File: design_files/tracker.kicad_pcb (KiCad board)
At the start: 4 copper layers, 49.4 x 53.4 mm, 88 parts, among them J1 Conn_01x01, J2 Conn_01x01, J3 Conn_01x05, J4 Conn_Coaxial, J5 SIM_Card, J6 Conn_01x02, M1 BG96, Q1 DMP2008UFG, U1 STM32U545CEUx, U10 PUMH10,115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

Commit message: Edits
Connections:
- U12 pad 2: /I2C_SDA -> +3V3
- U12 pad 3: unconnected-(U12-DOUT_A6-Pad3) -> +3V3
- U12 pad 4: unconnected-(U12-DIN_SDA-Pad4) -> /I2C_SDA
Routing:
- net +3V3: track 58.1 -> 61.1 mm
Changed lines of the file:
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@@
 	(net 144 "Net-(U11-~{QON})")
 	(net 145 "Net-(U11-~{CE})")
-	(net 146 "unconnected-(U12-DIN_SDA-Pad4)")
-	(net 147 "unconnected-(U12-NC-Pad5)")
-	(net 148 "unconnected-(U12-NC-Pad10)")
-	(net 149 "unconnected-(U12-INTN2-Pad11)")
-	(net 150 "unconnected-(U12-DOUT_A6-Pad3)")
-	(net 151 "unconnected-(U12-NC-Pad8)")
-	(net 152 "/accelerometer/ACC_INT1")
-	(net 153 "unconnected-(Y1-Pad2)")
-	(net 154 "unconnected-(Y1-Pad3)")
+	(net 146 "unconnected-(U12-NC-Pad5)")
+	(net 147 "unconnected-(U12-NC-Pad10)")
+	(net 148 "unconnected-(U12-INTN2-Pad11)")
+	(net 149 "unconnected-(U12-NC-Pad8)")
+	(net 150 "/accelerometer/ACC_INT1")
+	(net 151 "unconnected-(Y1-Pad2)")
+	(net 152 "unconnected-(Y1-Pad3)")
 	(footprint "Resistor_SMD:R_0603_1608Metric"
 		(layer "F.Cu")
@@
 			(layers "F.Cu" "F.Mask" "F.Paste")
 			(roundrect_rratio 0.25)
-			(net 153 "unconnected-(Y1-Pad2)")
+			(net 151 "unconnected-(Y1-Pad2)")
 			(pinfunction "2")
 			(pintype "passive+no_connect")
@@
 			(layers "F.Cu" "F.Mask" "F.Paste")
 			(roundrect_rratio 0.25)
-			(net 154 "unconnected-(Y1-Pad3)")
+			(net 152 "unconnected-(Y1-Pad3)")
 			(pinfunction "3")
 			(pintype "passive+no_connect")
@@
 			(layers "F.Cu" "F.Mask" "F.Paste")
 			(roundrect_rratio 0.25)
-			(net 152 "/accelerometer/ACC_INT1")
+			(net 150 "/accelerometer/ACC_INT1")
 			(pinfunction "PA8")
 			(pintype "bidirectional")
@@
 			(size 0.375 0.35)
 			(layers "B.Cu" "B.Mask" "B.Paste")
-			(net 133 "/I2C_SDA")
+			(net 6 "+3V3")
 			(pinfunction "CSN")
 			(pintype "input")
@@
 			(size 0.375 0.35)
 			(layers "B.Cu" "B.Mask" "B.Paste")
-			(net 150 "unconnected-(U12-DOUT_A6-Pad3)")
+			(net 6 "+3V3")
 			(pinfunction "DOUT_A6")
-			(pintype "output+no_connect")
+			(pintype "output")
 		)
 		(pad "4" smd rect
@@
 			(size 0.375 0.35)
 			(layers "B.Cu" "B.Mask" "B.Paste")
-			(net 146 "unconnected-(U12-DIN_SDA-Pad4)")
+			(net 133 "/I2C_SDA")
 			(pinfunction "DIN_SDA")
-			(pintype "input+no_connect")
+			(pintype "input")
 		)
 		(pad "5" smd rect
@@
 			(size 0.375 0.35)
 			(layers "B.Cu" "B.Mask" "B.Paste")
-			(net 147 "unconnected-(U12-NC-Pad5)")
+			(net 146 "unconnected-(U12-NC-Pad5)")
 			(pinfunction "NC")
 			(pintype "no_connect")
@@
 			(size 0.375 0.35)
 			(layers "B.Cu" "B.Mask" "B.Paste")
-			(net 151 "unconnected-(U12-NC-Pad8)")
+			(net 149 "unconnected-(U12-NC-Pad8)")
 			(pinfunction "NC")
 			(pintype "no_connect")
@@
 			(size 0.375 0.35)
 			(layers "B.Cu" "B.Mask" "B.Paste")
-			(net 148 "unconnected-(U12-NC-Pad10)")
+			(net 147 "unconnected-(U12-NC-Pad10)")
 			(pinfunction "NC")
 			(pintype "no_connect")
@@
 			(size 0.375 0.35)
 			(layers "B.Cu" "B.Mask" "B.Paste")
-			(net 149 "unconnected-(U12-INTN2-Pad11)")
+			(net 148 "unconnected-(U12-INTN2-Pad11)")
 			(pinfunction "INTN2")
 			(pintype "output+no_connect")
@@
 			(size 0.375 0.35)
 			(layers "B.Cu" "B.Mask" "B.Paste")
-			(net 152 "/accelerometer/ACC_INT1")
+			(net 150 "/accelerometer/ACC_INT1")
 			(pinfunction "INTN1")
 			(pintype "output")
@@
 	)
 	(via
-		(at 144.53 85.2)
+		(at 144.5 84.55)
 		(size 0.6)
 		(drill 0.3)
@@
 	)
 	(segment
+		(start 135.25 84.69)
+		(end 135.4 84.54)
+		(width 0.15)
+		(layer "F.Cu")
+		(net 6)
+	)
+	(segment
 		(start 158.1325 82.51)
 		(end 158.1325 81.3475)
@@
 	)
 	(segment
-		(start 135.25 84.69)
-		(end 135.27 84.71)
-		(width 0.15)
-		(layer "F.Cu")
-		(net 6)
-	)
-	(segment
 		(start 138.99 86.21)
 		(end 138.99 85.67)
@@
 	)
 	(segment
+		(start 135.4 84.54)
+		(end 135.4 84.15)
+		(width 0.15)
+		(layer "F.Cu")
+		(net 6)
+	)
+	(segment
 		(start 138.99 85.67)
 		(end 138.47 85.15)
@@
 	)
 	(via
-		(at 135.27 84.71)
+		(at 135.4 84.15)
 		(size 0.6)
 		(drill 0.3)
@@
 	)
 	(segment
+		(start 135.3 84.05)
+		(end 135.4 84.15)
+		(width 0.15)
+		(layer "B.Cu")
+		(net 6)
+	)
+	(segment
 		(start 142.47 76.8875)
 		(end 141.7675 76.8875)
@@
 	)
 	(segment
+		(start 134.3125 84.05)
+		(end 134.3785 83.984)
+		(width 0.15)
+		(layer "B.Cu")
+		(net 6)
+	)
+	(segment
 		(start 157.68 81.34)
 		(end 158.14 81.34)
@@
 	)
 	(segment
+		(start 135 84.55)
+		(end 135.4 84.15)
+		(width 0.15)
+		(layer "B.Cu")
+		(net 6)
+	)
+	(segment
 		(start 131.655 84.455)
 		(end 131.655 84.345)
@@
 	)
 	(segment
+		(start 134.3125 84.55)
+		(end 135 84.55)
+		(width 0.15)
+		(layer "B.Cu")
+		(net 6)
+	)
+	(segment
+		(start 134.3125 84.05)
+		(end 135.3 84.05)
+		(width 0.15)
+		(layer "B.Cu")
+		(net 6)
+	)
+	(segment
 		(start 131.655 84.345)
 		(end 131.95 84.05)
@@
 	)
 	(segment
-		(start 134.3785 83.984)
-		(end 137.580123 83.984)
+		(start 137.580123 83.984)
+		(end 137.926123 84.33)
 		(width 0.15)
 		(layer "B.Cu")
@@
 	)
 	(segment
-		(start 137.580123 83.984)
-		(end 137.926123 84.33)
+		(start 134.3125 85.05)
+		(end 135.45 85.05)
 		(width 0.15)
 		(layer "B.Cu")
@@
 	)
 	(segment
-		(start 134.3125 84.05)
-		(end 134.3785 83.984)
+		(start 135.45 85.05)
+		(end 136.516 83.984)
+		(width 0.15)
+		(layer "B.Cu")
+		(net 133)
+	)
+	(segment
+		(start 136.516 83.984)
+		(end 137.580123 83.984)
 		(width 0.15)
 		(layer "B.Cu")
@@
 		(width 0.15)
 		(layer "F.Cu")
-		(net 152)
+		(net 150)
 	)
 	(segment
@@
 		(width 0.15)
 		(layer "F.Cu")
-		(net 152)
+		(net 150)
 	)
 	(segment
@@
 		(width 0.15)
 		(layer "F.Cu")
-		(net 152)
+		(net 150)
 	)
 	(segment
@@
 		(width 0.15)
 		(layer "F.Cu")
-		(net 152)
+		(net 150)
 	)
 	(segment
@@
 		(width 0.15)
 		(layer "F.Cu")
-		(net 152)
+		(net 150)
 	)
 	(via
@@
 		(drill 0.3)
 		(layers "F.Cu" "B.Cu")
-		(net 152)
+		(net 150)
 	)
 	(segment
@@
 		(width 0.15)
 		(layer "B.Cu")
-		(net 152)
+		(net 150)
 	)
 	(segment
@@
 		(width 0.15)
 		(layer "B.Cu")
-		(net 152)
+		(net 150)
 	)
 	(segment
@@
 		(width 0.15)
 		(layer "B.Cu")
-		(net 152)
+		(net 150)
 	)
 	(segment
@@
 		(width 0.15)
 		(layer "B.Cu")
-		(net 152)
+		(net 150)
 	)
 	(segment
@@
 		(width 0.15)
 		(layer "B.Cu")
-		(net 152)
+		(net 150)
 	)
 	(segment
@@
 		(width 0.15)
 		(layer "B.Cu")
-		(net 152)
+		(net 150)
 	)
 	(zone

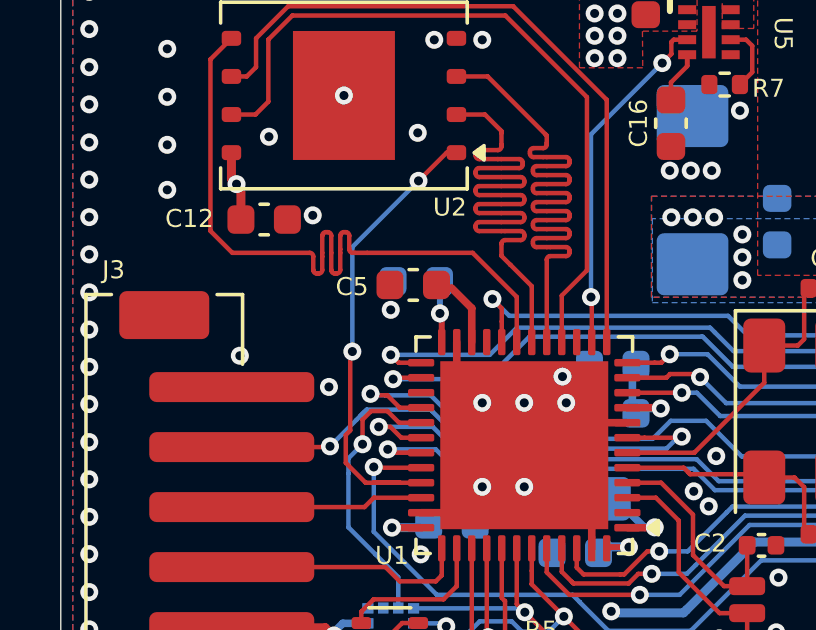
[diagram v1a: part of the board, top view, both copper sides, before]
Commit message: Added CS pullup
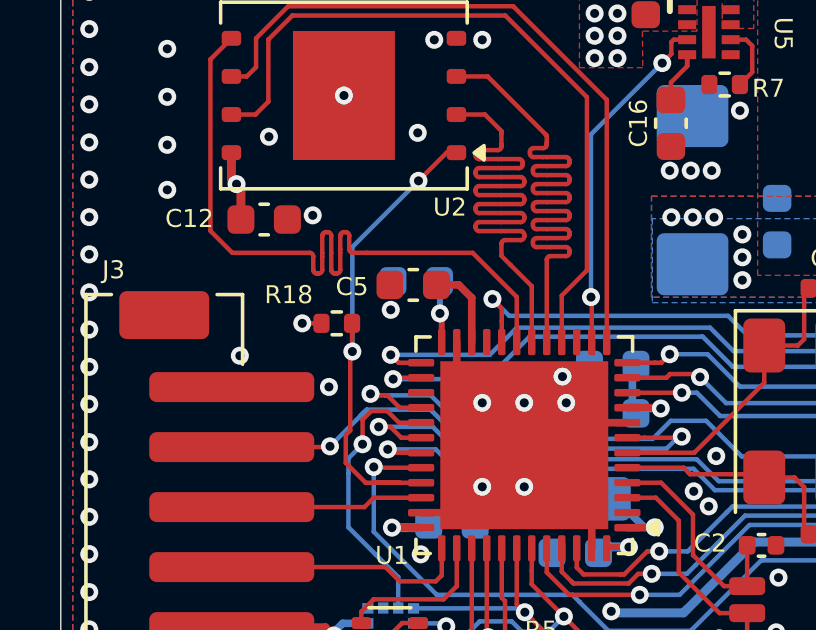
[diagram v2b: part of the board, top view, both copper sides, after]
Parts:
- added R18: 100K, Resistor_SMD:R_0402_1005Metric, F.Cu at (131.8, 74.0)
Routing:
- net /mcu/OCTOSPI1_NCS: track 15.8 -> 16.7 mm
- net /mcu/VCAP: track 2.08 -> 2.83 mm
- net +3V3: track 61.1 -> 61.8 mm, vias 16 -> 17
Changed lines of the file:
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@@
 	(footprint "Resistor_SMD:R_0402_1005Metric"
 		(layer "F.Cu")
+		(at 131.75 74.05)
+		(descr "Resistor SMD 0402 (1005 Metric), square (rectangular) end terminal, IPC-7351 nominal, (Body size source: IPC-SM-782 page 72, https://www.pcb-3d.com/wordpress/wp-content/uploads/ipc-sm-782a_amendment_1_and_2.pdf), generated with kicad-footprint-generator")
+		(tags "resistor")
+		(property "Reference" "R18"
+			(at -1.6 -0.95 0)
+			(layer "F.SilkS")
+			(effects
+				(font
+					(size 0.6 0.6)
+					(thickness 0.15)
+				)
+			)
+		)
+		(property "Value" "100K"
+			(at 0 1.17 0)
+			(layer "F.Fab")
+			(effects
+				(font
+					(size 1 1)
+					(thickness 0.15)
+				)
+			)
+		)
+		(property "Datasheet" "~"
+			(at 0 0 0)
+			(layer "F.Fab")
+			(hide yes)
+			(effects
+				(font
+					(size 1.27 1.27)
+					(thickness 0.15)
+				)
+			)
+		)
+		(property "Description" "Resistor, small symbol"
+			(at 0 0 0)
+			(layer "F.Fab")
+			(hide yes)
+			(effects
+				(font
+					(size 1.27 1.27)
+					(thickness 0.15)
+				)
+			)
+		)
+		(property ki_fp_filters "R_*")
+		(sheetname "/mcu/")
+		(sheetfile "mcu.kicad_sch")
+		(attr smd)
+		(fp_line
+			(start -0.153641 -0.38)
+			(end 0.153641 -0.38)
+			(stroke
+				(width 0.12)
+				(type solid)
+			)
+			(layer "F.SilkS")
+		)
+		(fp_line
+			(start -0.153641 0.38)
+			(end 0.153641 0.38)
+			(stroke
+				(width 0.12)
+				(type solid)
+			)
+			(layer "F.SilkS")
+		)
+		(fp_line
+			(start -0.93 -0.47)
+			(end 0.93 -0.47)
+			(stroke
+				(width 0.05)
+				(type solid)
+			)
+			(layer "F.CrtYd")
+		)
+		(fp_line
+			(start -0.93 0.47)
+			(end -0.93 -0.47)
+			(stroke
+				(width 0.05)
+				(type solid)
+			)
+			(layer "F.CrtYd")
+		)
+		(fp_line
+			(start 0.93 -0.47)
+			(end 0.93 0.47)
+			(stroke
+				(width 0.05)
+				(type solid)
+			)
+			(layer "F.CrtYd")
+		)
+		(fp_line
+			(start 0.93 0.47)
+			(end -0.93 0.47)
+			(stroke
+				(width 0.05)
+				(type solid)
+			)
+			(layer "F.CrtYd")
+		)
+		(fp_line
+			(start -0.525 -0.27)
+			(end 0.525 -0.27)
+			(stroke
+				(width 0.1)
+				(type solid)
+			)
+			(layer "F.Fab")
+		)
+		(fp_line
+			(start -0.525 0.27)
+			(end -0.525 -0.27)
+			(stroke
+				(width 0.1)
+				(type solid)
+			)
+			(layer "F.Fab")
+		)
+		(fp_line
+			(start 0.525 -0.27)
+			(end 0.525 0.27)
+			(stroke
+				(width 0.1)
+				(type solid)
+			)
+			(layer "F.Fab")
+		)
+		(fp_line
+			(start 0.525 0.27)
+			(end -0.525 0.27)
+			(stroke
+				(width 0.1)
+				(type solid)
+			)
+			(layer "F.Fab")
+		)
+		(fp_text user "${REFERENCE}"
+			(at 0 0 0)
+			(layer "F.Fab")
+			(effects
+				(font
+					(size 0.26 0.26)
+					(thickness 0.04)
+				)
+			)
+		)
+		(pad "1" smd roundrect
+			(at -0.51 0)
+			(size 0.54 0.64)
+			(layers "F.Cu" "F.Mask" "F.Paste")
+			(roundrect_rratio 0.25)
+			(net 6 "+3V3")
+			(pintype "passive")
+		)
+		(pad "2" smd roundrect
+			(at 0.51 0)
+			(size 0.54 0.64)
+			(layers "F.Cu" "F.Mask" "F.Paste")
+			(roundrect_rratio 0.25)
+			(net 89 "/mcu/OCTOSPI1_NCS")
+			(pintype "passive")
+		)
+		(embedded_fonts no)
+		(model "${KICAD9_3DMODEL_DIR}/Resistor_SMD.3dshapes/R_0402_1005Metric.step"
+			(offset
+				(xyz 0 0 0)
+			)
+			(scale
+				(xyz 1 1 1)
+			)
+			(rotate
+				(xyz 0 0 0)
+			)
+		)
+	)
+	(footprint "Resistor_SMD:R_0402_1005Metric"
+		(layer "F.Cu")
 		(at 144.68 66.09 180)
 		(descr "Resistor SMD 0402 (1005 Metric), square (rectangular) end terminal, IPC-7351 nominal, (Body size source: IPC-SM-782 page 72, https://www.pcb-3d.com/wordpress/wp-content/uploads/ipc-sm-782a_amendment_1_and_2.pdf), generated with kicad-footprint-generator")
@@
 	)
 	(segment
+		(start 131.24 74.05)
+		(end 130.6 74.05)
+		(width 0.15)
+		(layer "F.Cu")
+		(net 6)
+	)
+	(segment
 		(start 141.4375 76.8625)
 		(end 142.445 76.8625)
@@
 	)
 	(via
+		(at 130.6 74.05)
+		(size 0.6)
+		(drill 0.3)
+		(layers "F.Cu" "B.Cu")
+		(net 6)
+	)
+	(via
 		(at 142.55 76.8875)
 		(size 0.6)
@@
 	)
 	(segment
+		(start 132.26 74.98)
+		(end 132.27 74.99)
+		(width 0.15)
+		(layer "F.Cu")
+		(net 89)
+	)
+	(segment
 		(start 132.7125 79.3625)
 		(end 132.051 78.701)
@@
 	)
 	(segment
+		(start 132.26 74.05)
+		(end 132.26 74.98)
+		(width 0.15)
+		(layer "F.Cu")
+		(net 89)
+	)
+	(segment
 		(start 133.85 79.3625)
 		(end 133.55 79.3625)
@@
 	)
 	(segment
-		(start 136.25 73.545)
-		(end 135.575 72.87)
+		(start 136.25 74.675)
+		(end 136.25 73.2)
+		(width 0.254)
+		(layer "F.Cu")
+		(net 118)
+	)
+	(segment
+		(start 136.25 73.2)
+		(end 135.82 72.77)
 		(width 0.254)
 		(layer "F.Cu")
@@
 	)
 	(segment
-		(start 136.25 74.675)
-		(end 136.25 73.545)
+		(start 135.82 72.77)
+		(end 135.075 72.77)
 		(width 0.254)
 		(layer "F.Cu")

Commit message: First review.
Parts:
- added G***: LOGO, My_Footprints:bk_logo_10mm, F.Cu at (130.7, 56.7)
- added R19: 10K, Resistor_SMD:R_0402_1005Metric, F.Cu at (142.9, 84.7)
- added R20: 10K, Resistor_SMD:R_0402_1005Metric, F.Cu at (163.2, 77.5)
- R7: moved to B.Cu
- moved R7 1.71 mm to (144.9, 64.4), turned to -90 degrees
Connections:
- R7 pad 1: Net-(U5-DIS) -> /gsm/+GSM_SWITCHED
- R7 pad 2: GND -> Net-(U5-DIS)
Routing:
- net +3V3: track 61.8 -> 67.9 mm
- net /gsm/GSM_STATUS: track 28.7 -> 30.1 mm
- net /gsm/+GSM_SWITCHED: track 0.00 -> 0.84 mm, vias 0 -> 1
- net Net-(U5-DIS): track 2.26 -> 2.67 mm, vias 0 -> 1
- net GND: vias 335 -> 333
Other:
- board text added: "BK Telematics TraceLink R1"
